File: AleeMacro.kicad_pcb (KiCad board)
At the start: 2 copper layers, 265.4 x 111.2 mm, 50 parts, among them SW1 SW_Push, U1 ProMicro

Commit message: Named and Logo Imported
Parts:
- added G***: LOGO, locallib:aelogo, F.Cu at (-8.89, 85.1)
- OLED: value Conn_01x04_Male (OLED) -> Conn_01x04
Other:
- board text added: "GND"
- board text added: "He touched the butt."
- board text added: "SCL"
- board text added: "SDA"
- board text added: "VCC"
- board text removed: "This is the butt."

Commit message: Ground Fills Added & Edges Thinned
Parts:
- moved G*** 166.8 mm to (147.3, 26.7)
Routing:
- net COL2: track 109.9 -> 116.6 mm
- net ROW2: track 83.8 -> 89.5 mm
- net ROW0: track 103.8 -> 108.9 mm, vias 0 -> 2
- net SDA: track 25.0 -> 28.0 mm, vias 0 -> 1
- net COL1: track 124.5 -> 126.9 mm
- net ROW1: track 95.1 -> 97.0 mm, vias 0 -> 2
- net Net-(D2-Pad2): track 35.9 -> 36.8 mm
- net ROW4: track 148.3 -> 149.1 mm
- added copper zone on B.Cu, net GND
- added copper zone on F.Cu, net GND
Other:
- board size 265.4 x 111.2 mm -> 245.1 x 101.1 mm

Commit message: Edgecut and Standoff clearence - Solved
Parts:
- removed G***: LOGO, locallib:aelogo
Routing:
- net VCC: track 26.4 -> 27.0 mm
- net ROW1: vias 2 -> 3
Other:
- board size 245.1 x 101.1 mm -> 245.1 x 103.6 mm
- board text added: "AleeMacro"
- board text removed: "Vendor/Customizing instructions 1. Fork Soyuz on GitHub to create your own copy. Clone onto your PC. 2. Turn your logo into a footprint using bitmap2component, save in locallib.pretty. 3. Place it on the topside of the bottom plate. It is left intentionally blank for this. 4. Alt+3 to render and see if it looks nice. 5. Using the Plot tool, generate the gerbers. The bottom plate is reversible."

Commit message: Designs added
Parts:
- added G***: LOGO, locallib:woofer2, F.Cu at (82.5, 95.2)
- added G***: LOGO, locallib:woofer2, F.Cu at (63.5, 104.1)
- added G***: LOGO, locallib:woofer2, F.Cu at (50.8, 87.6)
- added G***: LOGO, locallib:woofer2, F.Cu at (69.8, 78.7)
- added G***: LOGO, locallib:alee9-mini, F.Cu at (175.3, 52.1)
- moved D2 0.57 mm to (134.9, 62.7)
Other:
- board text added: "AleeMacro Plate V1.0"
- board text removed: "AleeMacro V1.0"

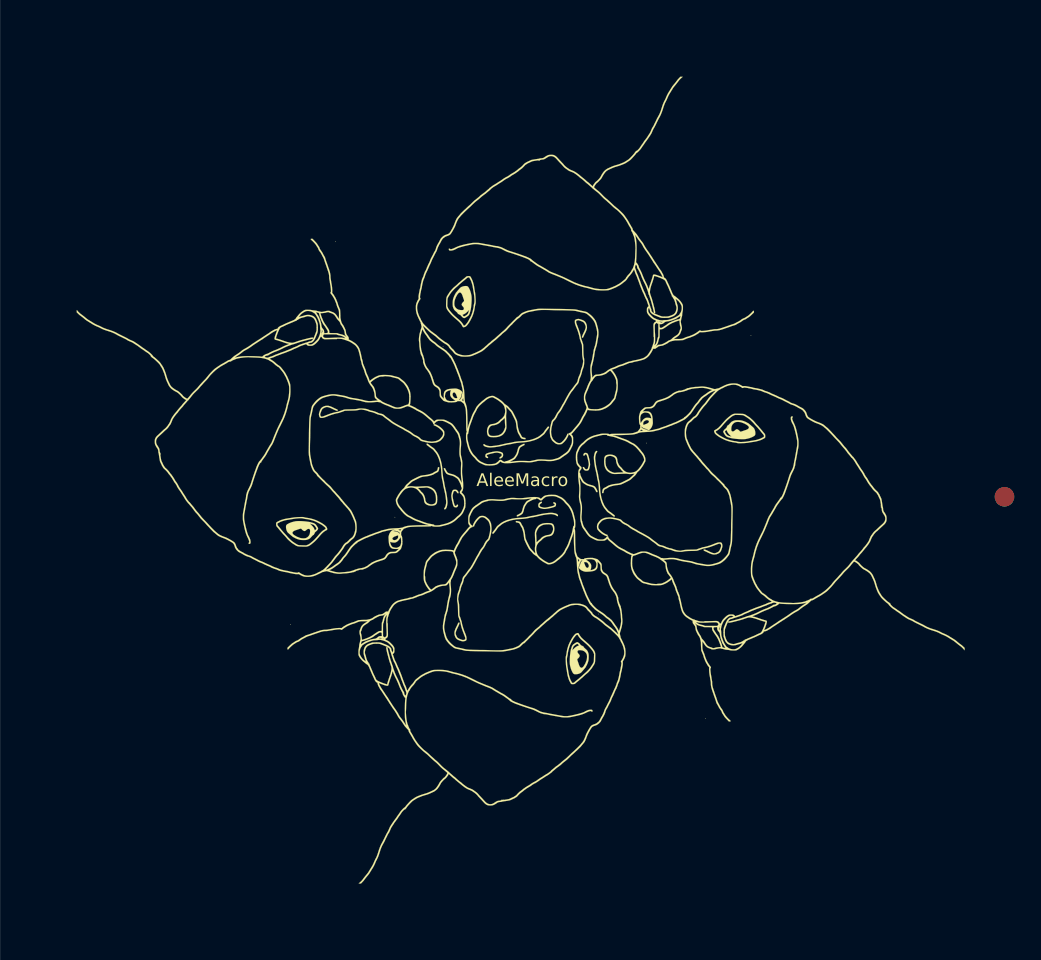
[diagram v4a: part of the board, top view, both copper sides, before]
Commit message: Plate Design Updated
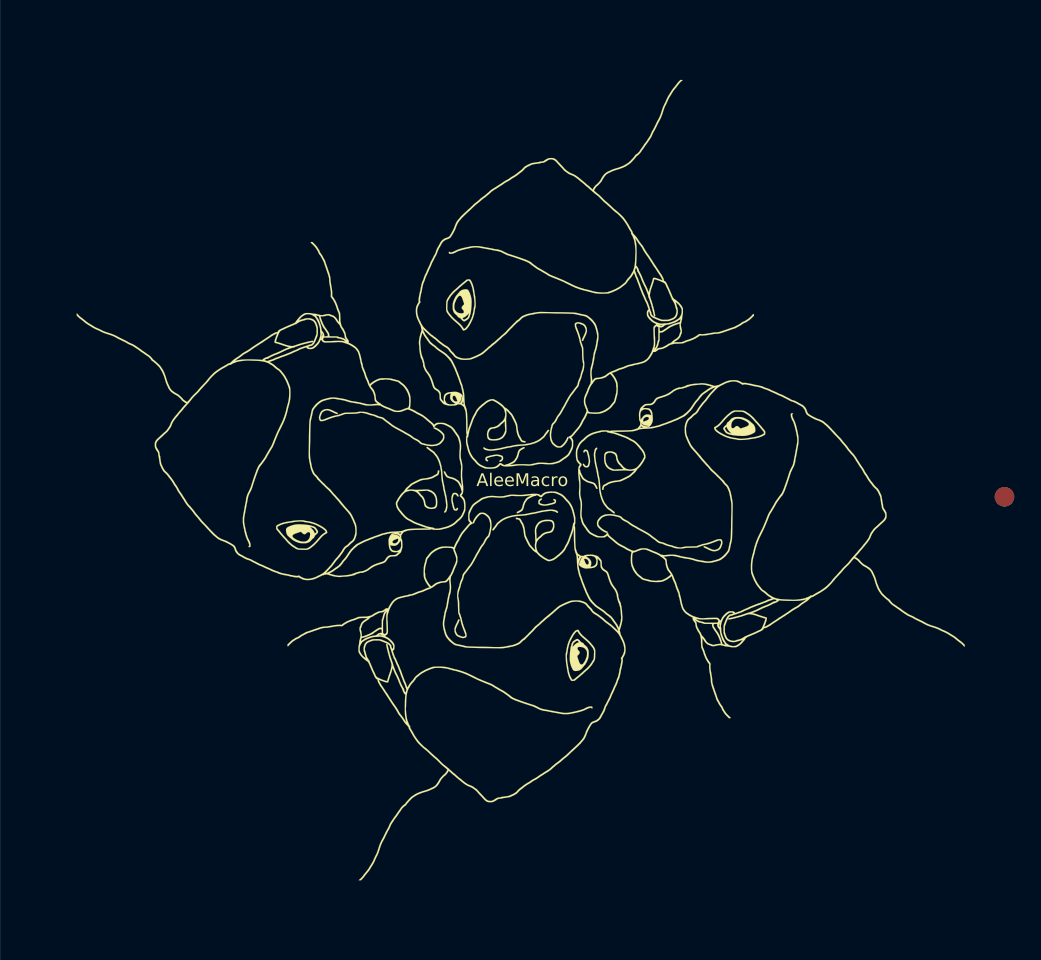
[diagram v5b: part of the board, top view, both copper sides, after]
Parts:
- removed the G*** at (82.5, 95.2)
- removed the G*** at (63.5, 104.1)
- removed the G*** at (50.8, 87.6)
- removed the G*** at (69.8, 78.7)
- added G***: LOGO, locallib:woofer3, F.Cu at (50.8, 87.9)
- added G***: LOGO, locallib:woofer3, F.Cu at (63.5, 103.9)
- added G***: LOGO, locallib:woofer3, F.Cu at (69.8, 79.0)
- added G***: LOGO, locallib:woofer3, F.Cu at (82.5, 95.0)

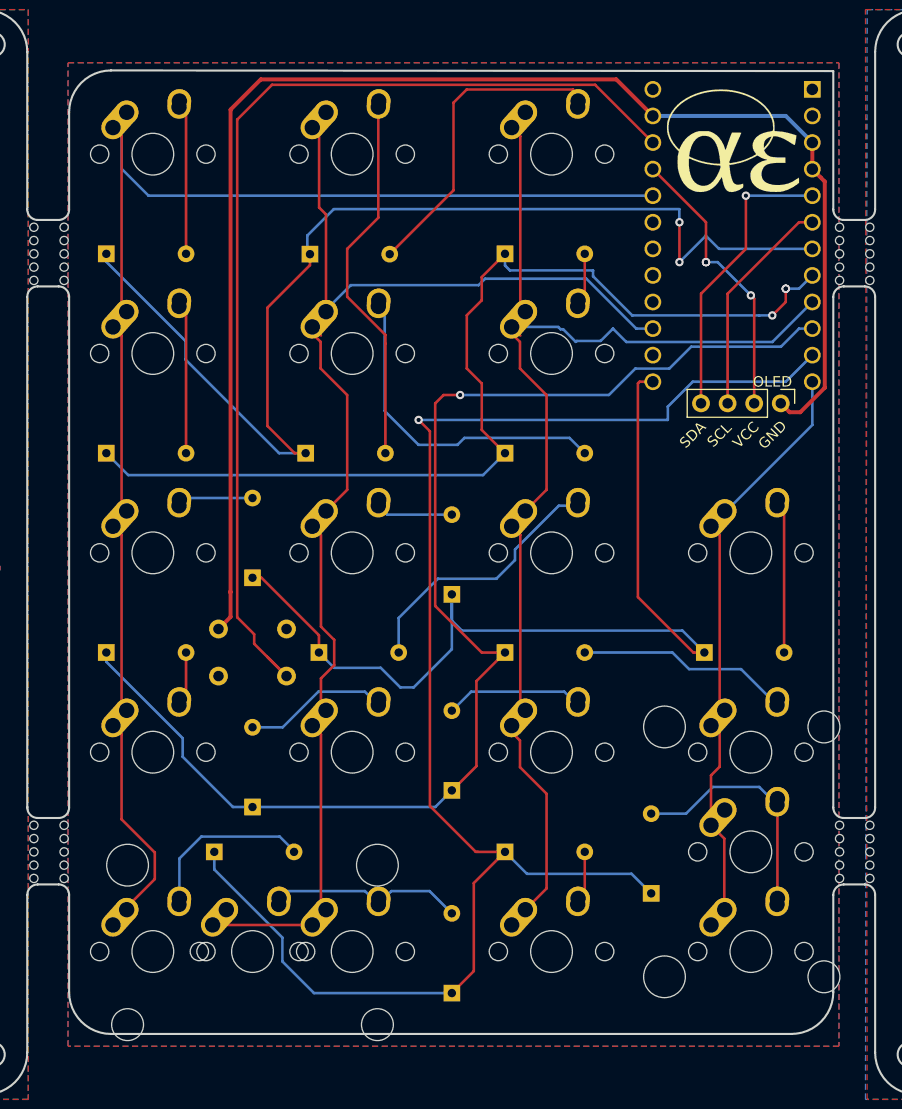
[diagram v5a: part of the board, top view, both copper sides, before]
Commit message: Improved diode placement and Routing
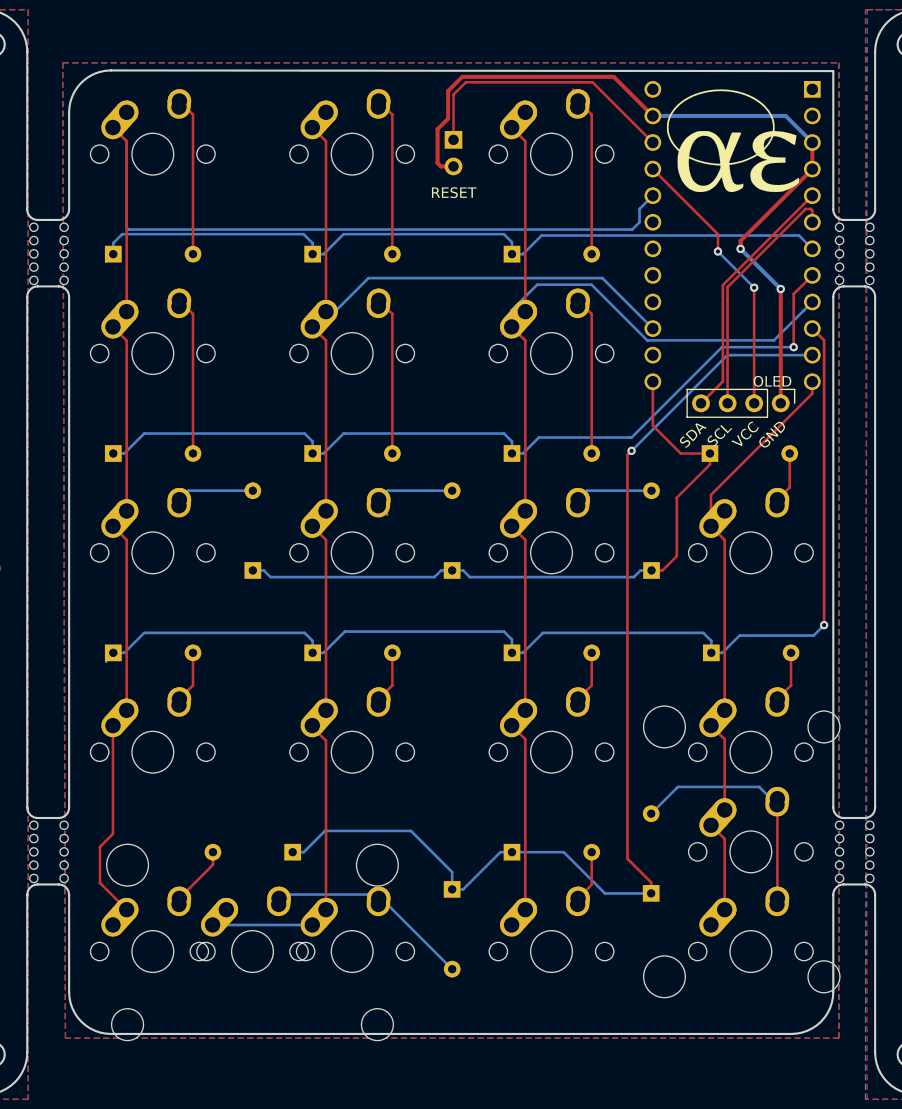
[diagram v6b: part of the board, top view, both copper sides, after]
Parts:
- Reset: renamed from SW1; value SW_Push -> RESET; footprint random-keyboard-parts:PushButton_6x6mm_TH_Pretty -> Connector_PinHeader_2.54mm:PinHeader_1x02_P2.54mm_Vertical
- moved Reset 52.6 mm to (148.6, 51.8), turned to 180 degrees
- moved D9 32.7 mm to (167.5, 93.0), turned to 90 degrees
- moved D14 19.7 mm to (173.2, 100.8)
- moved D3 19.3 mm to (154.2, 62.7)
- moved D6 19.1 mm to (154.2, 81.8)
- moved D2 19.0 mm to (135.1, 62.7)
- moved D10 19.0 mm to (173.1, 81.8)
- moved D5 18.4 mm to (135.1, 81.8)
- moved D12 15.8 mm to (135.1, 100.8), turned to 0 degrees
- moved D13 14.3 mm to (154.2, 100.8), turned to 0 degrees
- moved D16 9.91 mm to (148.5, 123.4), turned to 270 degrees
- moved D15 7.49 mm to (133.2, 119.9), turned to 180 degrees
- moved D8 2.29 mm to (148.5, 93.0)
- moved D7 0.70 mm to (129.4, 93.0)
- moved D1 0.67 mm to (116.1, 62.7)
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- renumbered D12 to D10, D13 to D11, D14 to D12, D15 to D13, D16 to D14, D17 to D15, D18 to D16, D19 to D17, D20 to D18, D6 to D2, D2 to D3, D5 to D4, D7 to D5, D3 to D6, D9 to D7, D10 to D8, D11 to D9, MX12 to MX10, MX13 to MX11, MX14 to MX12, MX15 to MX13, MX16 to MX14, MX17 to MX15, MX18 to MX16, MX21 to MX16a, MX19 to MX17, MX20 to MX18, MX22 to MX18a, MX5 to MX4, MX6 to MX5, MX7 to MX6, MX9 to MX7, MX10 to MX8, MX11 to MX9
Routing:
- net Net-(SW1-Pad1): track 101.1 -> 26.2 mm
- net GND: track 138.9 -> 76.3 mm, vias 0 -> 2
- net ROW4: track 149.1 -> 105.9 mm
- net ROW0: track 108.5 -> 73.9 mm, vias 2 -> 0
- net ROW2: track 89.5 -> 64.0 mm
- net Net-(D2-Pad2): track 36.8 -> 16.0 mm
- net Net-(D11-Pad2): track 25.4 -> 7.37 mm
- net ROW3: track 123.5 -> 105.6 mm
- net ROW1: track 97.0 -> 81.3 mm, vias 3 -> 1
- net Net-(D6-Pad2): track 31.6 -> 16.0 mm
- net Net-(D16-Pad2): track 20.5 -> 4.95 mm
- net Net-(D3-Pad2): track 31.5 -> 16.8 mm
- net Net-(D7-Pad2): track 4.71 -> 15.9 mm
- net Net-(D17-Pad2): track 16.3 -> 6.34 mm
- net Net-(D12-Pad2): track 14.3 -> 5.85 mm
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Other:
- board text added: "RESET"
